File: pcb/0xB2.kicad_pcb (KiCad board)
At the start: 2 copper layers, 17.8 x 33 mm, 42 parts, among them J1 USB_C_Receptacle_USB2.0, J2 Conn_01x12, J3 Conn_01x05, J4 Conn_01x12, J5 Conn_01x01, SW1 SW_Push, SW2 SW_Push, U1 RP2040, U2 W25Q32JVZP, U3 XC6210B332MR-G, Y1 Crystal_GND24

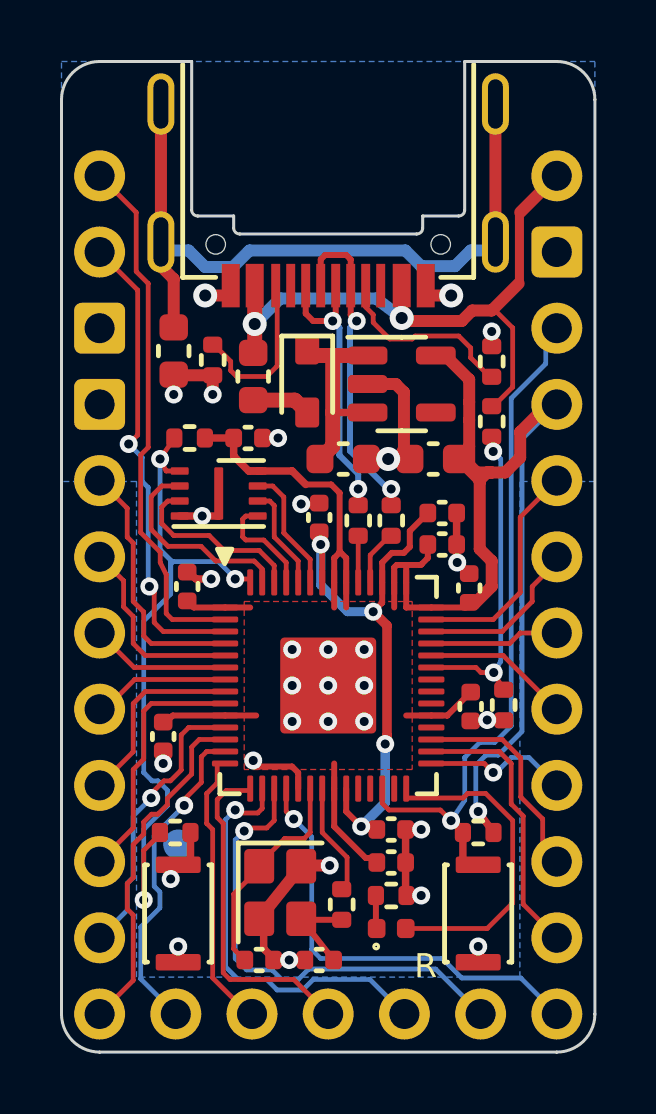
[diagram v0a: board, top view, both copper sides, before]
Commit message: Break out 5V instead of VBUS + routing update
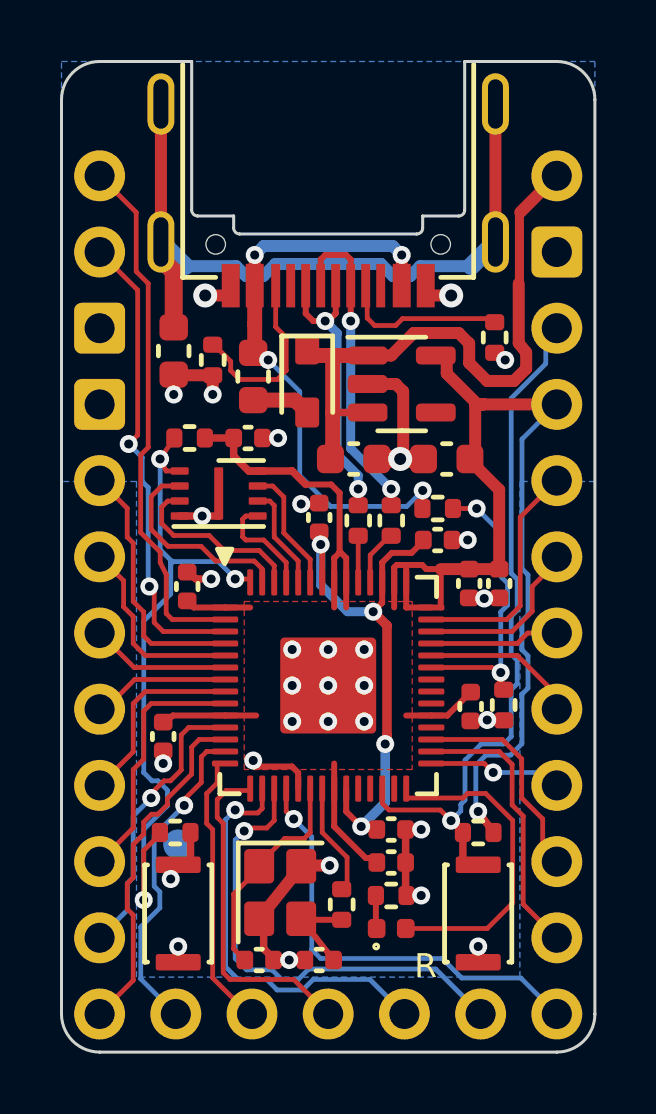
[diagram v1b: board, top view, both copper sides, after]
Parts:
- moved R10 3.41 mm to (156.1, 91.1), turned to 180 degrees
- moved C5 2.30 mm to (158.1, 93.6), turned to -90 degrees
- moved C6 0.91 mm to (156.1, 92.2)
- moved R4 0.81 mm to (157.9, 85.4), turned to -90 degrees
- moved C2 0.45 mm to (156.3, 89.5)
- moved C1 0.35 mm to (153.2, 89.5)
- moved C11 0.15 mm to (157.1, 93.6), turned to -90 degrees
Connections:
- J4 pad 12: VBUS -> +5V
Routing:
- net +5V: track 6.88 -> 20.5 mm
- net GND: track 30.7 -> 29.0 mm, vias 29 -> 30
- net VBUS: track 21.1 -> 19.5 mm, vias 2 -> 4
- net +3V3: track 61.5 -> 60.1 mm
- net +1V1: track 19.2 -> 18.3 mm
- net Net-(J1-PadA5): track 6.31 -> 5.60 mm
- net /VBUS_DET: track 10.4 -> 9.75 mm
- net Net-(J1-PadB5): track 5.61 -> 6.21 mm
- net /~{RESET}: track 22.9 -> 23.4 mm
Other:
- board text added: "v2"
- board text removed: "v1"

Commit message: Make the pinout compatible with KB2040
WARNING !!! Breaks the compatibility with v1
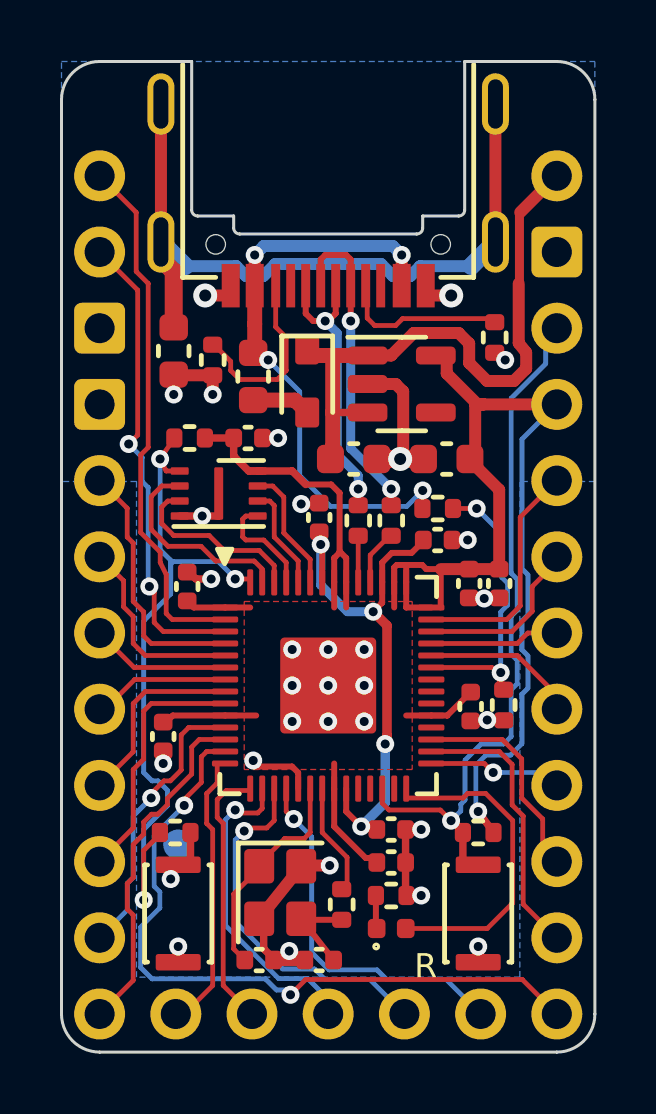
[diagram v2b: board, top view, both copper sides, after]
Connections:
- J3 pad 1: /D10 -> /D11
- J3 pad 2: /D11 -> /D12
- J3 pad 3: /D12 -> /D13
- J3 pad 4: /D13 -> /D14
- J3 pad 5: /D14 -> /D15
- J4 pad 1: /D15 -> /D10
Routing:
- net /D10: track 10.9 -> 23.8 mm, vias 1 -> 2
- net /D14: track 15.8 -> 12.3 mm
- net /D13: track 13.9 -> 10.6 mm
- net /D15: track 14.8 -> 12.3 mm
- net /D12: track 11.2 -> 9.03 mm
- net GND: track 29.0 -> 30.3 mm

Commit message: Minor routing changes
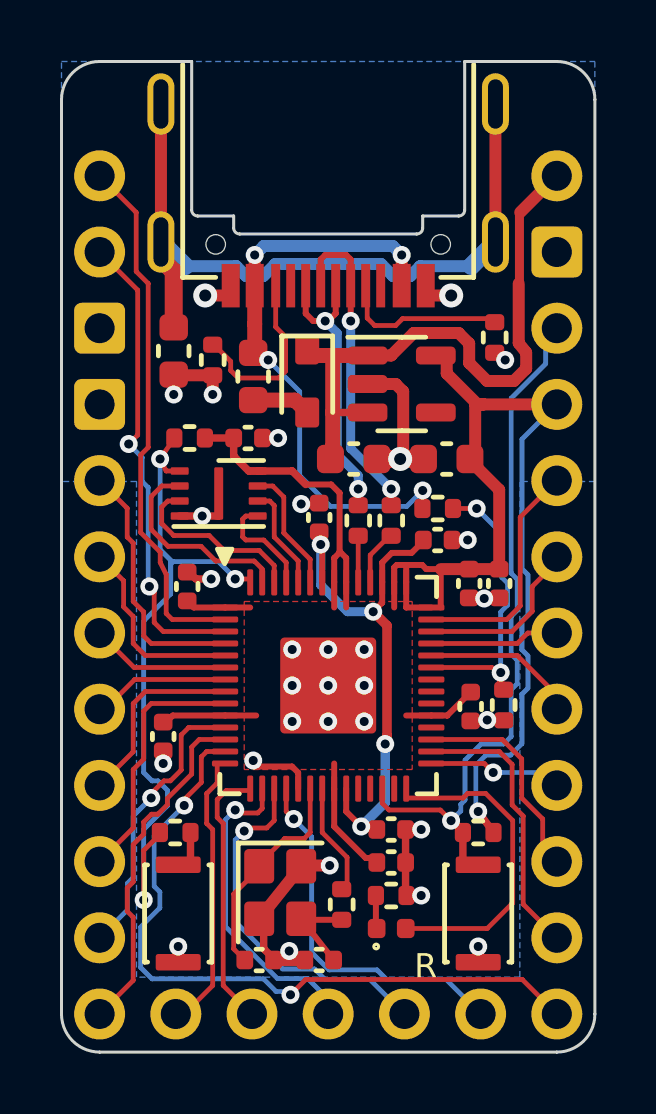
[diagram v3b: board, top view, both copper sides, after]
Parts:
- removed J5: Conn_01x01, TestPoint:TestPoint_Pad_D1.0mm
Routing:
- net Net-(R3-Pad1): track 3.14 -> 1.38 mm, vias 1 -> 0

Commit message: Change to Sparkfun RP2040 pinout
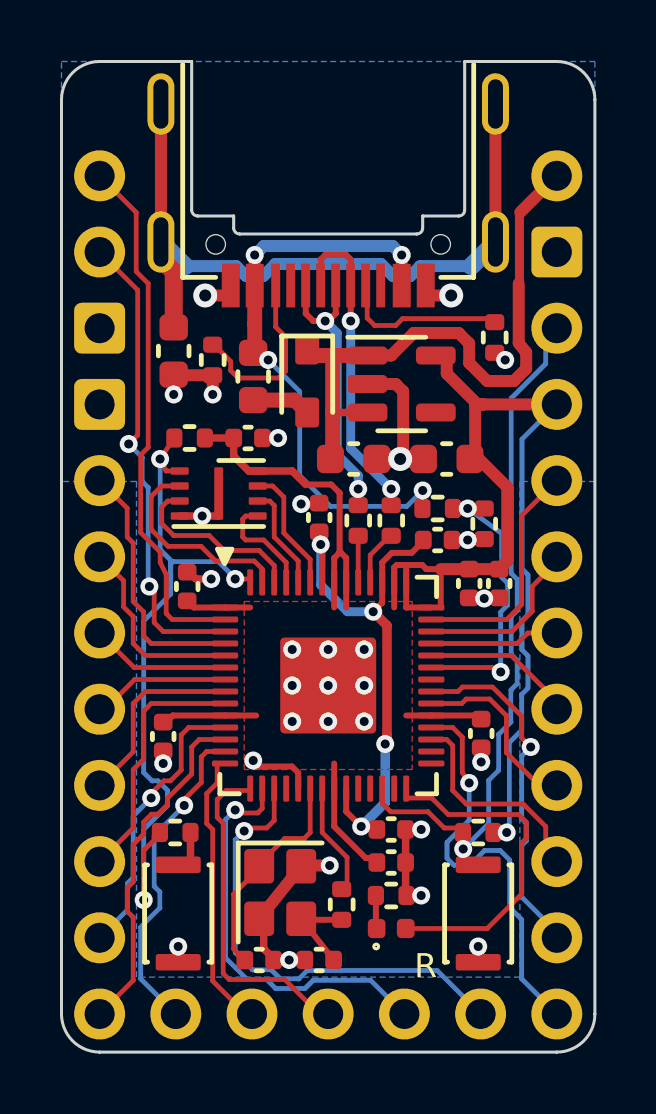
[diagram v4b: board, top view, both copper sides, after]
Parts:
- moved R11 6.07 mm to (157.6, 91.6)
- moved C13 0.97 mm to (157.5, 98.6)
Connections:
- J3 pad 1: /D11 -> /D10
- J3 pad 2: /D12 -> /D11
- J3 pad 3: /D13 -> /D12
- J3 pad 4: /D14 -> /D13
- J3 pad 5: /D15 -> /D14
- J4 pad 1: /D10 -> /D21
- U1 pad 18: /D15 -> unconnected-(U1-Pad18)
- U1 pad 29: /SCLK -> unconnected-(U1-Pad29)
- U1 pad 30: /MOSI -> unconnected-(U1-Pad30)
- U1 pad 32: unconnected-(U1-Pad32) -> /D21
- U1 pad 34: unconnected-(U1-Pad34) -> /SCLK
- U1 pad 35: unconnected-(U1-Pad35) -> /MOSI
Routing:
- net /D21: track 0.00 -> 13.9 mm, vias 0 -> 1
- net /D10: track 23.8 -> 11.2 mm, vias 2 -> 1
- net /D15: track 12.3 -> 0.00 mm, vias 1 -> 0
- net /D14: track 12.3 -> 15.6 mm
- net /D13: track 10.6 -> 13.7 mm
- net /D12: track 9.03 -> 11.7 mm
- net /MOSI: track 9.27 -> 11.7 mm, vias 0 -> 1
- net /SCLK: track 4.48 -> 6.16 mm, vias 1 -> 0
- net /~{RESET}: track 23.4 -> 24.9 mm
- net GND: track 30.3 -> 29.5 mm
- net +3V3: track 60.1 -> 59.6 mm
